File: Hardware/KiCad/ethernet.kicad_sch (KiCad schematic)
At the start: 16 parts, among them J2 RJ45_Hanrun_HR911105A_Horizon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, J3 RJ45_Hanrun_HR911105A_Horizon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, J4 RJ45_Hanrun_HR911105A_Horizon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, J7 RJ45_Hanrun_HR911105A_Horizon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

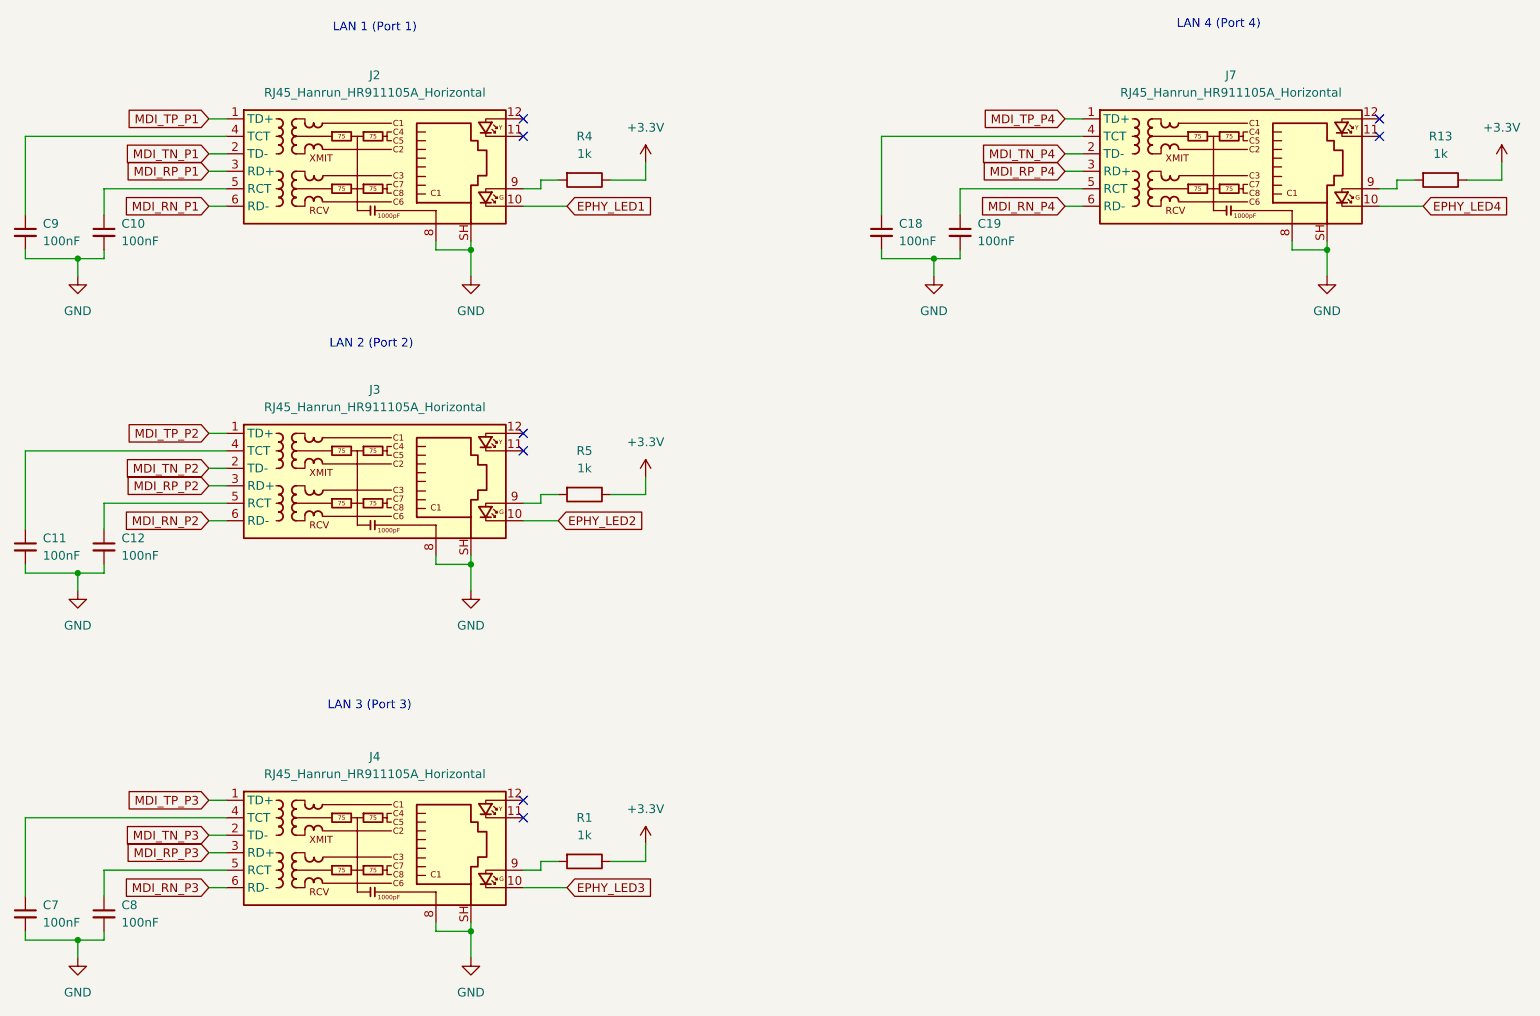
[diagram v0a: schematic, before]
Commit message: Rename all MDI signals to match kicad diffpair naming scheme
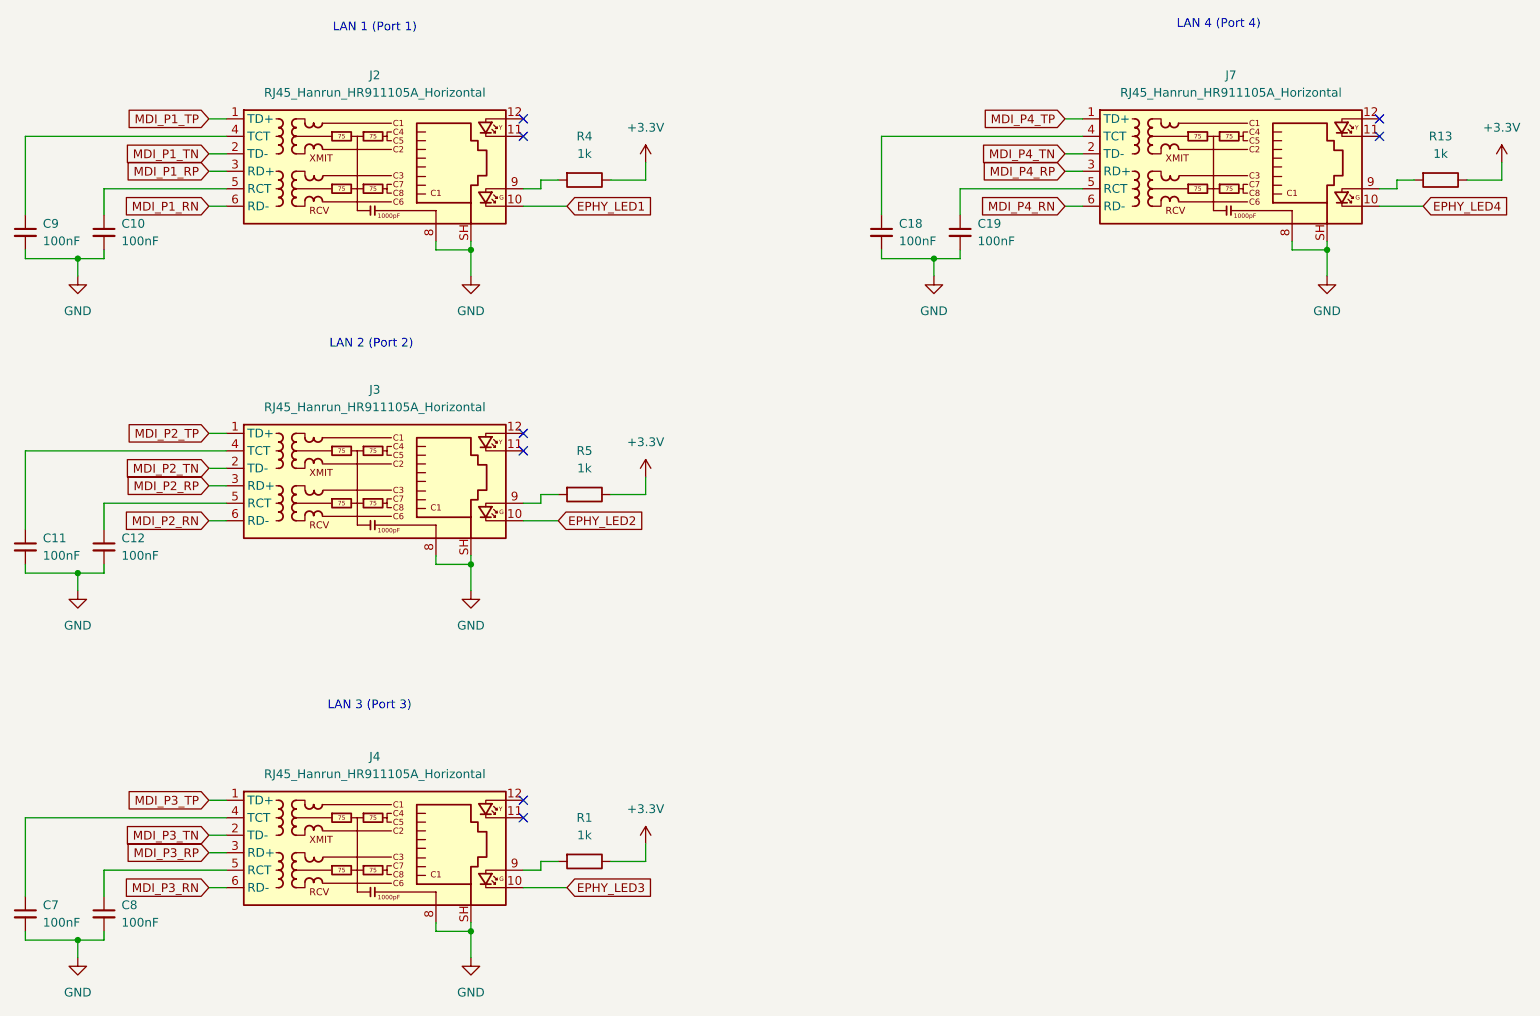
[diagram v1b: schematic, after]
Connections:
- net MDI_RN_P1 renamed MDI_P1_RN
- net MDI_RN_P2 renamed MDI_P2_RN
- net MDI_RN_P3 renamed MDI_P3_RN
- net MDI_RN_P4 renamed MDI_P4_RN
- net MDI_RP_P1 renamed MDI_P1_RP
- net MDI_RP_P2 renamed MDI_P2_RP
- net MDI_RP_P3 renamed MDI_P3_RP
- net MDI_RP_P4 renamed MDI_P4_RP
- net MDI_TN_P1 renamed MDI_P1_TN
- net MDI_TN_P2 renamed MDI_P2_TN
- net MDI_TN_P3 renamed MDI_P3_TN
- net MDI_TN_P4 renamed MDI_P4_TN
- net MDI_TP_P1 renamed MDI_P1_TP
- net MDI_TP_P2 renamed MDI_P2_TP
- net MDI_TP_P3 renamed MDI_P3_TP
- net MDI_TP_P4 renamed MDI_P4_TP
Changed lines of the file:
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@@
 		)
 	)
-	(global_label "MDI_TP_P2"
+	(global_label "MDI_P2_TP"
 		(shape input)
 		(at 77.47 83.82 180)
@@
 		)
 	)
-	(global_label "MDI_RN_P4"
+	(global_label "MDI_P4_RN"
 		(shape input)
 		(at 201.93 50.8 180)
@@
 		)
 	)
-	(global_label "MDI_RP_P3"
+	(global_label "MDI_P3_RP"
 		(shape input)
 		(at 77.47 144.78 180)
@@
 		)
 	)
-	(global_label "MDI_RN_P3"
+	(global_label "MDI_P3_RN"
 		(shape input)
 		(at 77.47 149.86 180)
@@
 		)
 	)
-	(global_label "MDI_RP_P1"
+	(global_label "MDI_P1_RP"
 		(shape input)
 		(at 77.47 45.72 180)
@@
 		)
 	)
-	(global_label "MDI_TP_P1"
+	(global_label "MDI_P1_TP"
 		(shape input)
 		(at 77.47 38.1 180)
@@
 		)
 	)
-	(global_label "MDI_RP_P4"
+	(global_label "MDI_P4_RP"
 		(shape input)
 		(at 201.93 45.72 180)
@@
 		)
 	)
-	(global_label "MDI_RN_P2"
+	(global_label "MDI_P2_RN"
 		(shape input)
 		(at 77.47 96.52 180)
@@
 		)
 	)
-	(global_label "MDI_TP_P4"
+	(global_label "MDI_P4_TP"
 		(shape input)
 		(at 201.93 38.1 180)
@@
 		)
 	)
-	(global_label "MDI_RP_P2"
+	(global_label "MDI_P2_RP"
 		(shape input)
 		(at 77.47 91.44 180)
@@
 		)
 	)
-	(global_label "MDI_TN_P3"
+	(global_label "MDI_P3_TN"
 		(shape input)
 		(at 77.47 142.24 180)
@@
 		)
 	)
-	(global_label "MDI_TN_P1"
+	(global_label "MDI_P1_TN"
 		(shape input)
 		(at 77.47 43.18 180)
@@
 		)
 	)
-	(global_label "MDI_TN_P2"
+	(global_label "MDI_P2_TN"
 		(shape input)
 		(at 77.47 88.9 180)
@@
 		)
 	)
-	(global_label "MDI_TP_P3"
+	(global_label "MDI_P3_TP"
 		(shape input)
 		(at 77.47 137.16 180)
@@
 		)
 	)
-	(global_label "MDI_RN_P1"
+	(global_label "MDI_P1_RN"
 		(shape input)
 		(at 77.47 50.8 180)
@@
 		)
 	)
-	(global_label "MDI_TN_P4"
+	(global_label "MDI_P4_TN"
 		(shape input)
 		(at 201.93 43.18 180)

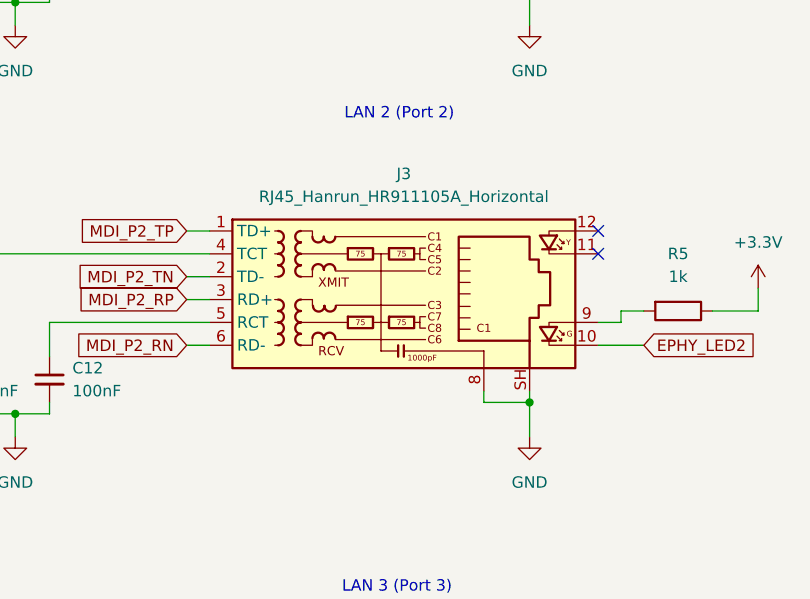
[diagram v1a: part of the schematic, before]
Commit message: Hardware: Lay out and route GPIO Header, USB and some other stuff
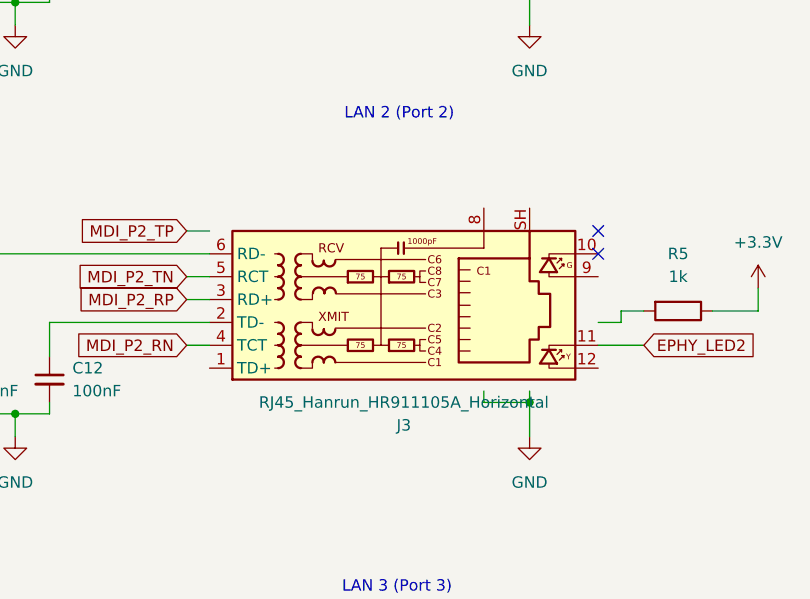
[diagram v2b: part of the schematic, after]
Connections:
- net EPHY_LED2: now also J3.11; no longer J3.10
- net GND: no longer J3.8, J3.SH
- net MDI_P2_RN: now also J3.4 (TCT); no longer J3.6 (RD-)
- net MDI_P2_TN: now also J3.5 (RCT); no longer J3.2 (TD-)
- net MDI_P2_TP: no longer J3.1 (TD+)
- net at R5.2: no longer J3.9
- net at C11.1: now also J3.6 (RD-); no longer J3.4 (TCT)
- net at C12.1: now also J3.2 (TD-); no longer J3.5 (RCT)
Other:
- moved on the sheet: J3
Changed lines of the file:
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@@
 		(lib_id "Connector:RJ45_Hanrun_HR911105A_Horizontal")
 		(at 100.33 91.44 0)
+		(mirror x)
 		(unit 1)
 		(body_style 1)
@@
 		(in_pos_files yes)
 		(dnp no)
-		(fields_autoplaced yes)
 		(property "Reference" "J3"
-			(at 101.6 77.47 0)
+			(at 101.6 105.41 0)
 			(show_name no)
 			(do_not_autoplace no)
@@
 		)
 		(property "Value" "RJ45_Hanrun_HR911105A_Horizontal"
-			(at 101.6 80.01 0)
+			(at 101.6 102.87 0)
 			(show_name no)
 			(do_not_autoplace no)
@@
 		)
 		(property "Footprint" "Connector_RJ:RJ45_Hanrun_HR911105A_Horizontal"
-			(at 100.33 78.74 0)
+			(at 100.33 104.14 0)
 			(hide yes)
 			(show_name no)
@@
 		)
 		(property "Datasheet" "https://datasheet.lcsc.com/lcsc/1811141815_HANRUN-Zhongshan-HanRun-Elec-HR911105A_C12074.pdf"
-			(at 100.33 76.2 0)
+			(at 100.33 106.68 0)
 			(hide yes)
 			(show_name no)
